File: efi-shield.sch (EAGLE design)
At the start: 155 parts, among them J1 PWMH, J10 MOLEX-85505-5002, J2 PWMI, J3 COMM, J4 PWR, J5 ADCL, J6 ADCH, J7 AMPSEAL-23POS-HEADER, J8 SPI, J9 MOLEX-85505-5002, Q1 PN2222A, Q2 FJPF13009, Q3 PN2222A, Q4 PN2222A, Q5 PN2222A, Q6 PN2222A, Q7 ISL9V5036P3_F085, SW1 CTS-204-211ST, U1 TXS0104E, U10 MCP2551-I/SN, U2 TXS0104E, U3 MCP3304, U4 MCP6024, U5 MCP6024

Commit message: Changed analog input filters + tach circuit.
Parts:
- removed C10, C11, C12, C20, C21, C22, C9: 330pF, cpsmv:CAP-JKE
- removed C23: 2.2uF, cpsmv:CAP-JKE
- removed C24: 0.1uF, cpsmv:CAP-JKE
- removed C25: 68nF, cpsmv:CAP-JKE
- removed JP4: SPR_A1, cpsmv:PINHD-1X1
- removed JP5: SPR_A2, cpsmv:PINHD-1X1
- removed JP6: SPR_A3, cpsmv:PINHD-1X1
- removed R39, R40, R41, R42, R43, R44: 0Ω, cpsmv:RES-JKE
- removed TP14: CS3_3V3, cpsmv:TEST-POINT
- removed TP15: CS2_3V3, cpsmv:TEST-POINT
- removed TP20: MAP, cpsmv:TEST-POINT
- removed TP21: MAP_FIL, cpsmv:TEST-POINT
- removed TP22: TPS, cpsmv:TEST-POINT
- removed TP23: TPS_FIL, cpsmv:TEST-POINT
- removed TP24: IAT, cpsmv:TEST-POINT
- removed TP25: IAT_FIL, cpsmv:TEST-POINT
- removed TP26: ECT, cpsmv:TEST-POINT
- removed TP27: ECT_FIL, cpsmv:TEST-POINT
- removed TP28: O2, cpsmv:TEST-POINT
- removed TP29: O2_FIL, cpsmv:TEST-POINT
- removed TP30: SPR_A1, cpsmv:TEST-POINT
- removed TP31: SPR_A1_FIL, cpsmv:TEST-POINT
- removed TP32: SPR_A2, cpsmv:TEST-POINT
- removed TP33: SPR_A2_FIL, cpsmv:TEST-POINT
- removed TP34: SPR_A3, cpsmv:TEST-POINT
- removed TP35: SPR_A3_FIL, cpsmv:TEST-POINT
- removed TP52: CS2_5V, cpsmv:TEST-POINT
- removed TP53: CS3_5V, cpsmv:TEST-POINT
- removed U3: MCP3304, cpsmv:MCP3304-CI/SL
- removed U4: MCP6024, cpsmv:MCP6024-E/SL
- added R18, R71, R74, R80, R83, R89: 120kΩ, cpsmv:RES-JKE
- added R19, R72, R81, R90: 56kΩ, cpsmv:RES-JKE
- added R64: 220Ω, cpsmv:RES-JKE
- added R65: 390Ω, cpsmv:RES-JKE
- added R66, R75, R84: 68kΩ, cpsmv:RES-JKE
- added R67, R76, R85: 3.9kΩ, cpsmv:RES-JKE
- added R68, R77, R86: 39kΩ, cpsmv:RES-JKE
- added R69, R70, R78, R79, R87, R88: 82kΩ, cpsmv:RES-JKE
- added R73, R82: 180kΩ, cpsmv:RES-JKE
- added U7, U8, U9: LM358, cpsmv:LM358
- C13: value 330pF -> 6.8nF
- C14, C5: value 47nF -> 10nF
- C16, C18: value 330pF -> 10nF
- C3: value 0.1uF -> 10nF
- C4: value 0.1uF -> 47nF
- C6: value 330pF -> 47nF
- R10: value 100kΩ -> 56kΩ
- R11, R2: value 100kΩ -> 180kΩ
- R12, R3, R9: value 100kΩ -> 120kΩ
- R13, R4: value 100kΩ -> 68kΩ
- R14, R5: value 100kΩ -> 3.9kΩ
- R15, R6: value 100kΩ -> 39kΩ
- R16, R17, R7, R8: value 100kΩ -> 330kΩ
- R20: value 220Ω -> 180kΩ
- R21: value 390Ω -> 120kΩ
- R37, R38: value 0Ω -> 680Ω
- U2: value TXS0104E -> LM358; device cpsmv:TXS0104ED -> cpsmv:LM358
- U5: value MCP6024 -> LM358; device cpsmv:MCP6024-E/SL -> cpsmv:LM358
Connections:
- removed net CS2_3V3: TP15.TP, U2.A1
- removed net CS2_5V: TP52.TP, U2.B1
- removed net CS3_3V3: TP14.TP, U2.A2
- removed net CS3_5V: TP53.TP, U2.B2
- removed net ECT_ADC: R40.2, U3.CH3
- removed net IAT_ADC: R39.2, U3.CH2
- removed net MAP_ADC: R37.2, U3.CH0
- removed net N$15: C15.2, R10.2, R11.1
- removed net N$16: C18.1, R13.2, U5.VINB+
- removed net N$17: C17.2, R12.2, R13.1
- removed net N$18: C20.1, R15.2, U5.VINC+
- removed net N$19: C19.2, R14.2, R15.1
- removed net N$20: C22.1, R17.2, U5.VIND+
- removed net N$21: C21.2, R16.2, R17.1
- removed net O2_ADC: R41.2, U3.CH4
- removed net SPRA1ADC: R42.2, U3.CH5
- removed net SPRA2ADC: R43.2, U3.CH6
- removed net SPRA3ADC: R44.2, U3.CH7
- removed net SPR_A1: JP4.1, R12.1, TP30.TP
- removed net SPR_A1_FIL: C17.1, R42.1, TP31.TP, U5.VINB-, U5.VOUTB
- removed net SPR_A2: JP5.1, R14.1, TP32.TP
- removed net SPR_A2_FIL: C19.1, R43.1, TP33.TP, U5.VINC-, U5.VOUTC
- removed net SPR_A3: JP6.1, R16.1, TP34.TP
- removed net SPR_A3_FIL: C21.1, R44.1, TP35.TP, U5.VIND-, U5.VOUTD
- removed net TPS_ADC: R38.2, U3.CH1
- new net N$13: C6.1, R16.2, R17.2, U2.VINB-
- new net N$4: R10.2, R9.2, U5.VINB+
- new net N$53: R66.2, R67.2, U7.VINA+
- new net N$54: R71.2, R72.2, U7.VINB+
- new net N$55: R20.2, R21.2, U7.VINA-
- new net N$56: R21.1, R69.1, U7.VOUTA
- new net N$57: C15.1, R69.2, R70.2, U7.VINB-
- new net N$58: R67.1, R68.2
- new net N$59: R75.2, R76.2, U8.VINA+
- new net N$60: R80.2, R81.2, U8.VINB+
- new net N$61: R73.2, R74.2, U8.VINA-
- new net N$62: R74.1, R78.1, U8.VOUTA
- new net N$63: C17.1, R78.2, R79.2, U8.VINB-
- new net N$64: R76.1, R77.2
- new net N$65: R84.2, R85.2, U9.VINA+
- new net N$66: R89.2, R90.2, U9.VINB+
- new net N$67: R82.2, R83.2, U9.VINA-
- new net N$68: R83.1, R87.1, U9.VOUTA
- new net N$69: C19.1, R87.2, R88.2, U9.VINB-
- new net N$70: R85.1, R86.2
- net +3V3: no longer C4.1, U2.VCCA
- net +5V: now also C16.1, C18.1, R13.1, R18.1, R37.2, R38.2, R4.1, R64.2, R66.1, R71.1, R75.1, R80.1, R84.1, R89.1, R9.1, U2.VDD, U7.VDD, U8.VDD, U9.VDD; no longer C23.1, C24.1, R20.2, U2.VCCB, U3.VDD, U3.VREF, U4.VDD
- net AGND: no longer C11.2, C13.2, C14.2, C16.2, C18.2, C20.2, C22.2, C23.2, C24.2, C5.2, C7.2, C9.2, U3.AGND, U3.DGND, U4.VSS, U5.VSS
- net CS1_5V: no longer U3.*CS/SHDN
- net ECT: now also C7.1, R2.1, R37.1; no longer R8.1, TP26.TP
- net ECT_FIL: now also C4.2, R8.1, U5.VOUTB; no longer C12.1, R40.1, TP27.TP, U4.VIND-, U4.VOUTD
- net GND: now also C13.2, C14.2, C16.2, C18.2, C5.2, C7.2, C8.2, R10.1, R15.1, R19.1, R6.1, R65.1, R68.1, R72.1, R77.1, R81.1, R86.1, R90.1, U2.VSS, U5.VSS, U7.VSS, U8.VSS, U9.VSS; no longer C25.2, C4.2, R21.1, U2.GND
- net HALL: now also C13.1, R64.1, R65.2; no longer C25.1, R20.1, R21.2
- net IAT: now also C8.1, R11.1, R38.1; no longer R6.1, TP24.TP
- net IAT_FIL: now also C6.2, R17.1, U2.VOUTB; no longer C10.1, R39.1, TP25.TP, U4.VINC-, U4.VOUTC
- net MAP: now also R20.1; no longer R2.1, TP20.TP
- net MAP_FIL: now also C15.2, R70.1, U7.VOUTB; no longer C6.1, R37.1, TP21.TP, U4.VINA-, U4.VOUTA
- net MISO_5V: no longer U3.DOUT
- net MOSI_5V: no longer U3.DIN
- net N$10: now also R18.2, R19.2, U2.VINB+; no longer C13.1, R9.2, U4.VIND+
- net N$11: now also R11.2, R12.2, U2.VINA-; no longer C12.2, R8.2, R9.1
- net N$12: now also R12.1, R16.1, U2.VOUTA; no longer U2.OE
- net N$14: now also R14.1, R15.2; no longer C16.1, R11.2, U5.VINA+
- net N$2: now also R4.2, R5.2, U5.VINA+; no longer C7.1, R3.2, U4.VINA+
- net N$5: now also R3.2, U5.VINA-; no longer C6.2, R3.1
- net N$6: now also R3.1, R7.1, U5.VOUTA; no longer C9.1, R5.2, U4.VINB+
- net N$7: now also C4.1, R7.2, R8.2, U5.VINB-; no longer C8.2, R4.2, R5.1
- net N$8: now also R13.2, R14.2, U2.VINA+; no longer C11.1, R7.2, U4.VINC+
- net N$9: now also R5.1; no longer C10.2, R7.1
- net O2: now also R73.1; no longer R10.1, TP28.TP
- net O2_FIL: now also C17.2, R79.1, U8.VOUTB; no longer C15.1, R41.1, TP29.TP, U5.VINA-, U5.VOUTA
- net SCK_5V: no longer U3.CLK
- net TPS: now also R82.1; no longer R4.1, TP22.TP
- net TPS_FIL: now also C19.2, R88.1, U9.VOUTB; no longer C8.1, R38.1, TP23.TP, U4.VINB-, U4.VOUTB
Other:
- note added: "Analog"
- note added: "ECT"
- note added: "IAT"
- note added: "MAP"
- note added: "O2"
- note added: "TPS"
- note added: "Thermistors"
- note removed: "ADC"
- note removed: "Analog Inputs"
- note removed: "LAYOUT NOTE: Place bulk capacitor within 100mm of both MCP602x devices."
- note removed: "LAYOUT NOTE: Place decoupling cap as close as possible to the Vdd pin."
- note removed: "LOW PASS FILTERS"

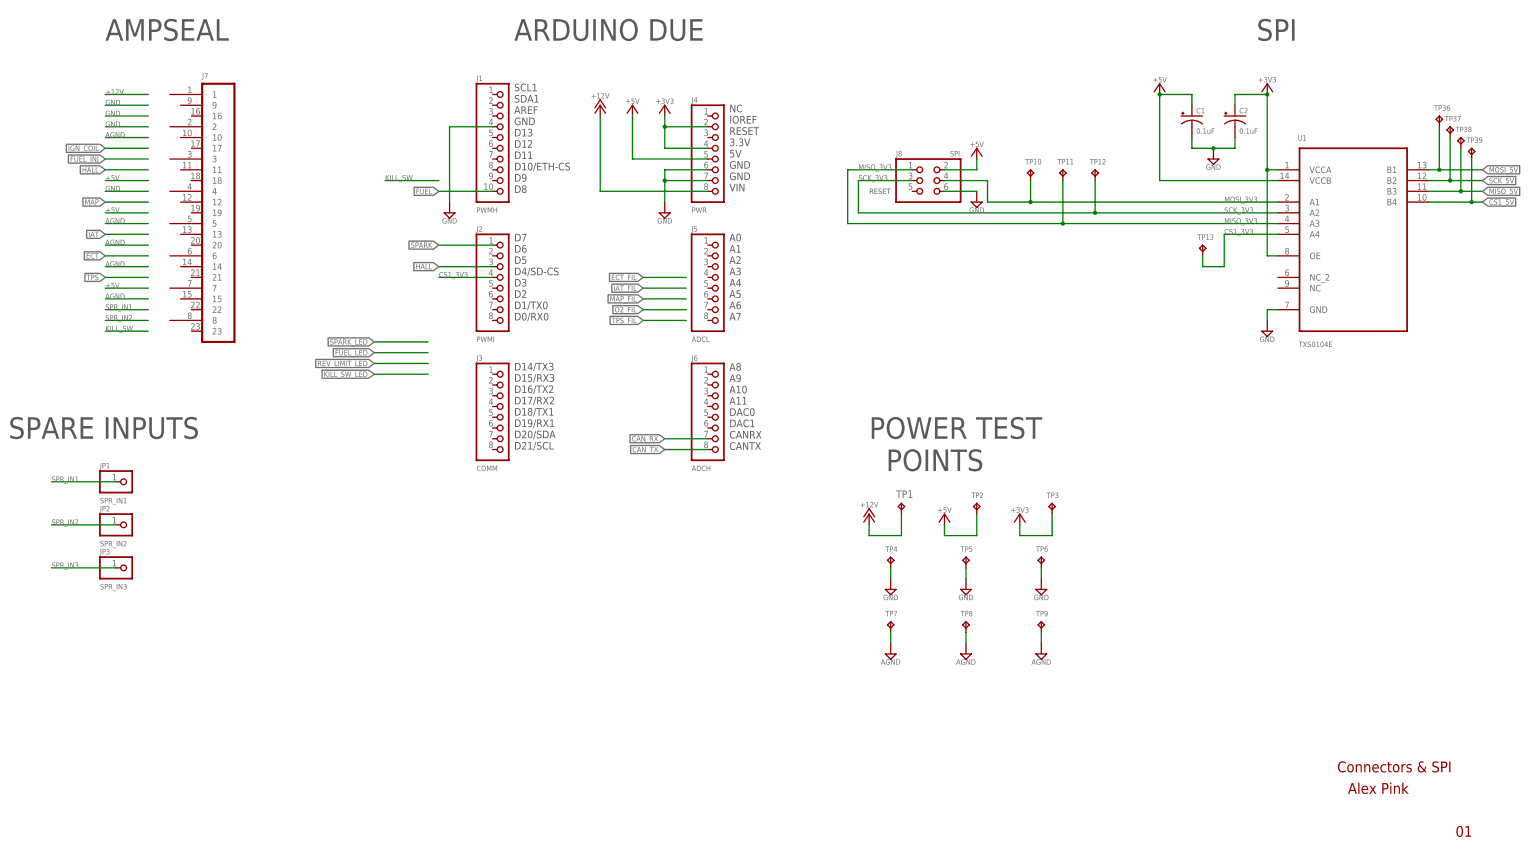
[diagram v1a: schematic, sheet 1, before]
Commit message: New test points, high frequency blocker for MAP, killswitch voltage divider.
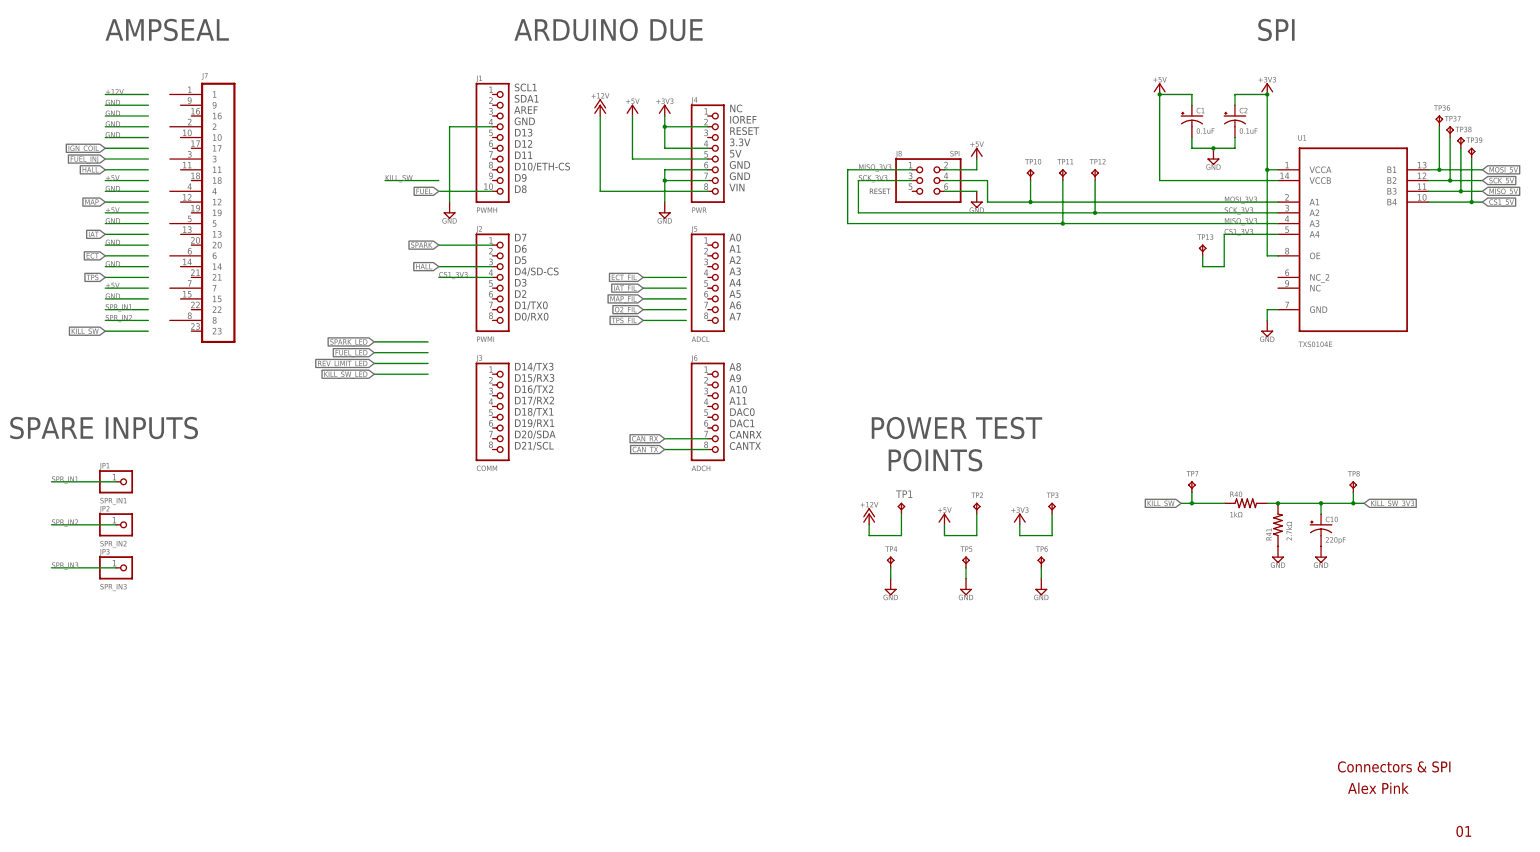
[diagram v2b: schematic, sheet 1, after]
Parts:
- removed TP9: AGND, cpsmv:TEST-POINT
- added C10: 220pF, cpsmv:CAP-JKE
- added C9: 330pF, cpsmv:CAP-JKE
- added R39: 470Ω, cpsmv:RES-JKE
- added R40: 1kΩ, cpsmv:RES-JKE
- added R41: 2.7kΩ, cpsmv:RES-JKE
- added TP14: HALL, cpsmv:TEST-POINT
- added TP15: ECT, cpsmv:TEST-POINT
- added TP20: ECT_FIL, cpsmv:TEST-POINT
- added TP21: IAT, cpsmv:TEST-POINT
- added TP22: IAT_FIL, cpsmv:TEST-POINT
- added TP23: MAP, cpsmv:TEST-POINT
- added TP24: MAP_FIL, cpsmv:TEST-POINT
- added TP25: O2, cpsmv:TEST-POINT
- added TP26: O2_FIL, cpsmv:TEST-POINT
- added TP27: TPS, cpsmv:TEST-POINT
- added TP28: TPS_FIL, cpsmv:TEST-POINT
- TP7: value AGND -> KILL_SW
- TP8: value AGND -> KILL_SW_3V3
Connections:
- removed net AGND: TP7.TP, TP8.TP, TP9.TP
- new net KILL_SW: R40.1, TP7.TP
- new net KILL_SW_3V3: C10.1, R40.2, R41.2, TP8.TP
- net ECT: now also TP15.TP
- net ECT_FIL: now also TP20.TP
- net GND: now also C10.2, C9.2, R39.1, R41.1
- net HALL: now also TP14.TP
- net IAT: now also TP21.TP
- net IAT_FIL: now also TP22.TP
- net MAP: now also C9.1, R39.2, TP23.TP
- net MAP_FIL: now also TP24.TP
- net O2: now also TP25.TP
- net O2_FIL: now also TP26.TP
- net TPS: now also TP27.TP
- net TPS_FIL: now also TP28.TP
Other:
- moved on the sheet: TP7, TP8
